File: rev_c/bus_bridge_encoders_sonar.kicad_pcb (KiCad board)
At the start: 2 copper layers, 100 x 50 mm, 52 parts, among them J1 POWER_SELECT, J2 TERMINATE_JUMPER, SW1 MJTP1243, U1 LM2940, U2 LTV-826, U3 LTV-826, U4 LTV-826, U5 754410, U6 LM2940, U7 74HCT08, U8 MCP2562, U9 ATMEGA328_DIP28, X1 16MHz

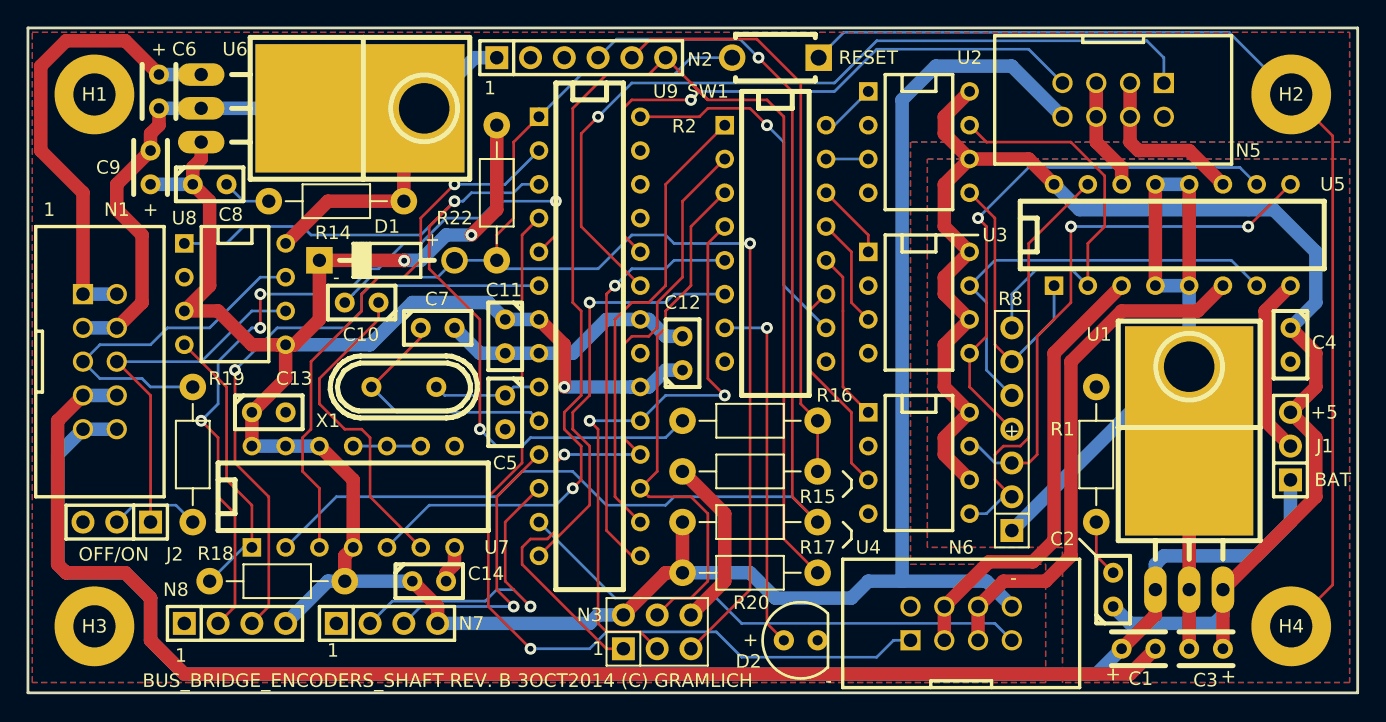
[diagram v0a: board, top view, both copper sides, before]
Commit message: Forgot to commit Rev. C.  Also changed vertical resistors to from pin_header to Resistor_Vertical__100 footprint.
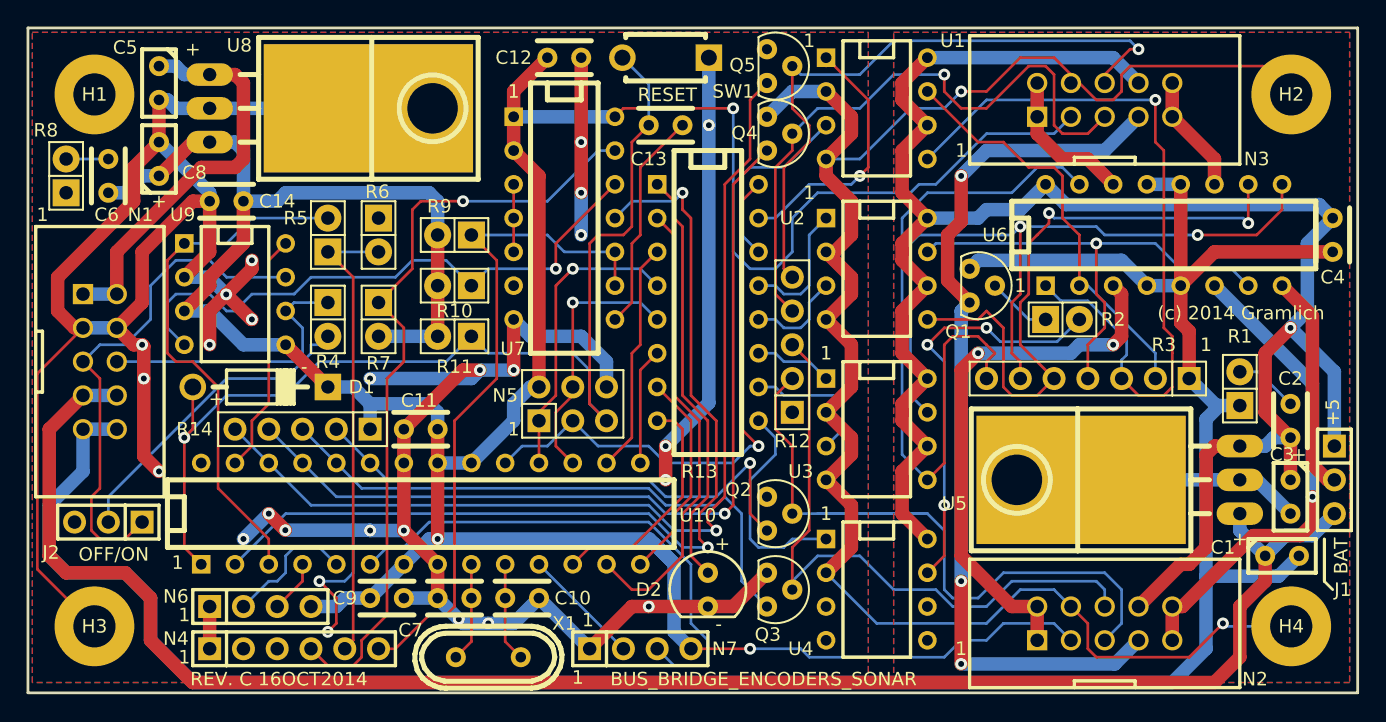
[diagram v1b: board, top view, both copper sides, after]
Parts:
- removed N8: HC_SR04_CONNECTOR, Bus_Bridge_Encoders_Sonar:Pin_Header_Straight_1x04
- removed R15: 22K, Bus_Bridge_Encoders_Sonar:Resistor_Horizontal_400
- removed R16: 33K, Bus_Bridge_Encoders_Sonar:Resistor_Horizontal_400
- removed R17, R18, R20: 100K, Bus_Bridge_Encoders_Sonar:Resistor_Horizontal_400
- removed R19: .47, Bus_Bridge_Encoders_Sonar:Resistor_Horizontal_400
- removed R22: 10K, Bus_Bridge_Encoders_Sonar:Resistor_Horizontal_400
- added N4: FTDI_HEADER, Bus_Bridge_Encoders_Sonar:Pin_Header_Straight_1x06, F.Cu at (120.0, 146.7)
- added Q1: PN2222, Bus_Bridge_Encoders_Sonar:TO92_123, F.Cu at (171.4, 119.4)
- added Q2: PN2222, Bus_Bridge_Encoders_Sonar:TO92_123, F.Cu at (156.2, 136.5)
- added Q3: PN2222, Bus_Bridge_Encoders_Sonar:TO92_123, F.Cu at (156.2, 142.2)
- added Q4: PN2222, Bus_Bridge_Encoders_Sonar:TO92_123, F.Cu at (156.2, 108.0)
- added Q5: PN2222, Bus_Bridge_Encoders_Sonar:TO92_123, F.Cu at (156.2, 102.9)
- added R10: 100K, Bus_Bridge_Encoders_Sonar:Pin_Header_Straight_1x02, F.Cu at (132.1, 119.4)
- added R11: 10K, Bus_Bridge_Encoders_Sonar:Pin_Header_Straight_1x02, F.Cu at (132.1, 123.2)
- added R12: 4K7x4, Bus_Bridge_Encoders_Sonar:Pin_Header_Straight_1x05, F.Cu at (157.5, 123.8)
- added R13: 470_DIP16, Bus_Bridge_Encoders_Sonar:DIP-16__300, F.Cu at (151.1, 120.7)
- added R3: 10Kx6, Bus_Bridge_Encoders_Sonar:Pin_Header_Straight_1x07, F.Cu at (179.7, 126.4)
- added R4: .47, Bus_Bridge_Encoders_Sonar:Pin_Header_Straight_1x02, F.Cu at (122.6, 121.9)
- added R5: 22K, Bus_Bridge_Encoders_Sonar:Pin_Header_Straight_1x02, F.Cu at (122.6, 115.6)
- added R6: 33K, Bus_Bridge_Encoders_Sonar:Pin_Header_Straight_1x02, F.Cu at (126.4, 115.6)
- added R7: 100K, Bus_Bridge_Encoders_Sonar:Pin_Header_Straight_1x02, F.Cu at (126.4, 121.9)
- added R9: 100K, Bus_Bridge_Encoders_Sonar:Pin_Header_Straight_1x02, F.Cu at (132.1, 115.6)
- added U10: ATMEGA328_DIP28, Bus_Bridge_Encoders_Sonar:DIP-28__300, F.Cu at (129.5, 136.5)
- C1, C3: footprint Bus_Bridge_Encoders_Sonar:Capacitor4x3RM2-5_RevB -> Bus_Bridge_Encoders_Sonar:Capacitor3MMDiscRM2.5
- C10: value .1uF -> 18pF; footprint Bus_Bridge_Encoders_Sonar:Capacitor3MMDiscRM2.5 -> Bus_Bridge_Encoders_Sonar:Capacitor4x3RM2-5_RevB
- C11, C12, C13, C14, C2, C4, C7: footprint Bus_Bridge_Encoders_Sonar:Capacitor3MMDiscRM2.5 -> Bus_Bridge_Encoders_Sonar:Capacitor4x3RM2-5_RevB
- C5: value 18pF -> 22uF
- C6, C9: value 22uF -> .1uF
- C8: value .1uF -> 22uF
- N2: value FTDI_HEADER -> MOTOR_ENCODER_CONN_2X5; footprint Bus_Bridge_Encoders_Sonar:Pin_Header_Straight_1x06 -> Bus_Bridge_Encoders_Sonar:Pin_Header_Straight_2x05_Shrouded
- N3: value AVR_ISP_HEADER -> MOTOR_ENCODER_CONN_2X5; footprint Bus_Bridge_Encoders_Sonar:Pin_Header_Straight_2x03 -> Bus_Bridge_Encoders_Sonar:Pin_Header_Straight_2x05_Shrouded
- N5: value MOTOR_ENCODER_CONN -> AVR_ISP_HEADER; footprint Bus_Bridge_Encoders_Sonar:Pin_Header_Straight_2x04_Shrouded -> Bus_Bridge_Encoders_Sonar:Pin_Header_Straight_2x03
- N6: value MOTOR_ENCODER_CONN -> HC_SR04_CONNECTOR; footprint Bus_Bridge_Encoders_Sonar:Pin_Header_Straight_2x04_Shrouded -> Bus_Bridge_Encoders_Sonar:Pin_Header_Straight_1x04
- R1: footprint Bus_Bridge_Encoders_Sonar:Resistor_Horizontal_400 -> Bus_Bridge_Encoders_Sonar:Pin_Header_Straight_1x02
- R14: value .47 -> 3K3x4; footprint Bus_Bridge_Encoders_Sonar:Resistor_Horizontal_400 -> Bus_Bridge_Encoders_Sonar:Pin_Header_Straight_1x05
- R2: value 470 -> 220; footprint Bus_Bridge_Encoders_Sonar:DIP-16__300 -> Bus_Bridge_Encoders_Sonar:Pin_Header_Straight_1x02
- R8: value 10K -> .47; footprint Bus_Bridge_Encoders_Sonar:Pin_Header_Straight_1x07 -> Bus_Bridge_Encoders_Sonar:Pin_Header_Straight_1x02
- U1: value LM2940 -> LTV-826; footprint Bus_Bridge_Encoders_Sonar:TO-220_Neutral123_Horizontal_LargePads -> Bus_Bridge_Encoders_Sonar:DIP-8__300
- U5: value 754410 -> LM2940; footprint Bus_Bridge_Encoders_Sonar:DIP-16__300 -> Bus_Bridge_Encoders_Sonar:TO-220_Neutral123_Horizontal_LargePads
- U6: value LM2940 -> 754410; footprint Bus_Bridge_Encoders_Sonar:TO-220_Neutral123_Horizontal_LargePads -> Bus_Bridge_Encoders_Sonar:DIP-16__300
- U8: value MCP2562 -> LM2940; footprint Bus_Bridge_Encoders_Sonar:DIP-8__300 -> Bus_Bridge_Encoders_Sonar:TO-220_Neutral123_Horizontal_LargePads
- U9: value ATMEGA328_DIP28 -> MCP2562; footprint Bus_Bridge_Encoders_Sonar:DIP-28__300 -> Bus_Bridge_Encoders_Sonar:DIP-8__300
- moved R8 73.6 mm to (102.9, 111.1)
- moved U6 73.0 mm to (185.4, 115.6), turned to 0 degrees
- moved N2 58.0 mm to (181.0, 144.8)
- moved N6 52.7 mm to (117.5, 143.5)
- moved N3 52.3 mm to (181.0, 105.4)
- moved N5 46.6 mm to (141.0, 128.3), turned to 0 degrees
- moved U1 43.2 mm to (163.8, 106.0), turned to 270 degrees
- moved C9 36.9 mm to (127.0, 142.9), turned to 0 degrees
- moved C13 36.8 mm to (148.0, 107.3), turned to 180 degrees
- moved C5 35.9 mm to (109.9, 104.1)
- moved C14 32.4 mm to (114.9, 113.0), turned to 180 degrees
- moved U9 26.9 mm to (115.6, 120.0)
- moved U7 26.3 mm to (140.3, 114.3), turned to 270 degrees
- moved C10 25.3 mm to (137.2, 142.9), turned to 0 degrees
- moved C12 23.9 mm to (140.3, 102.2), turned to 0 degrees
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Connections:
- C1 pad 1: /BPWR -> /Power/BPWR
- C1 pad 2: /BGND -> /Power/BGND
- C10 pad 2: /~RESET -> GND
- C13 pad 1: VCC -> Net-(C13-Pad1)
- C13 pad 2: GND -> /Logic/~RESET
- C2 pad 1: /M5V -> /Power/LED_5V
- C3 pad 1: /M5V -> /Power/LED_5V
- C3 pad 2: /BGND -> /Power/BGND
- C4 pad 1: /M5V -> /Power/LED_5V
- C4 pad 2: /BGND -> /Power/BGND
- C5 pad 1: Net-(C5-Pad1) -> /Logic/LPWR
- C6 pad 1: /LPWR -> VCC
- C6 pad 2: GND -> Net-(C6-Pad2)
- C8 pad 2: Net-(C8-Pad2) -> GND
- D1 pad +: /~RESET -> /Logic/~RESET
- J1 pad 1: /BPWR -> /Power/LED_5V
- J1 pad 2: /MOTOR_POWER -> /Power/MOTOR_POWER
- J1 pad 3: /M5V -> /Power/BPWR
- J2 pad 1: Net-(J2-Pad1) -> /Logic/CANH
- N1 pad 1: /LPWR -> /Logic/LPWR
- N1 pad 10: /BPWR -> /Power/BGND
- N1 pad 2: /LPWR -> /Logic/LPWR
- N1 pad 5: Net-(N1-Pad5) -> /Logic/CANH
- N1 pad 6: Net-(J2-Pad1) -> /Logic/CANL
- N1 pad 7: /BGND -> /Power/BPWR
- N1 pad 8: /BGND -> /Power/BPWR
- N1 pad 9: /BPWR -> /Power/BGND
- N2 pad 1: GND -> /Power/MOTOR1_A
- N2 pad 2: (no net) -> /Power/MOTOR1_A
- N2 pad 3: (no net) -> VCC
- N2 pad 4: Net-(N2-Pad4) -> GND
- N2 pad 5: Net-(N2-Pad5) -> /Logic/ENC1_A
- N2 pad 6: Net-(N2-Pad6) -> /Logic/ENC1_B
- N3 pad 1: /D12 -> /Power/MOTOR2_B
- N3 pad 2: VCC -> /Power/MOTOR2_B
- N3 pad 3: /D13 -> VCC
- N3 pad 4: /D11 -> GND
- N3 pad 5: /~RESET -> /Logic/ENC2_A
- N3 pad 6: GND -> /Logic/ENC2_B
- N5 pad 1: /A0 -> /Logic/D12
- N5 pad 2: GND -> VCC
- N5 pad 3: /M2+ -> /Logic/D13
- N5 pad 4: /M2+ -> /Logic/D11
- N5 pad 5: /M2- -> /Logic/~RESET
- N5 pad 6: /M2- -> GND
- N6 pad 1: /D2 -> GND
- N6 pad 2: GND -> /Logic/D3
- N6 pad 3: /M1+ -> /Logic/D2
- N6 pad 4: /M1+ -> VCC
- N7 pad 2: /D6 -> /Logic/D5
- N7 pad 3: /D5 -> /Logic/D4
- R1 pad 1: /BGND -> /Power/BGND
- R14 pad 1: GND -> VCC
- R14 pad 2: Net-(C8-Pad2) -> /Logic/A0
- R2 pad 1: /D10 -> Net-(Q1-Pad2)
- R2 pad 2: /D12 -> Net-(R2-Pad2)
- R8 pad 1: /BGND -> GND
- R8 pad 2: Net-(R8-Pad2) -> Net-(C6-Pad2)
- SW1 pad 2: /~RESET -> /Logic/~RESET
- U1 pad 1: /BPWR -> /Logic/1A
- U1 pad 2: /BGND -> GND
- U1 pad 3: /M5V -> /Logic/EN12
- U2 pad 1: Net-(R2-Pad16) -> /Logic/2A
- U2 pad 3: Net-(R2-Pad15) -> /Logic/3A
- U2 pad 5: Net-(R8-Pad6) -> Net-(R3-Pad5)
- U2 pad 6: /M5V -> /Power/LED_5V
- U2 pad 7: Net-(R8-Pad7) -> Net-(R3-Pad4)
- U2 pad 8: /M5V -> /Power/LED_5V
- U3 pad 1: Net-(R2-Pad14) -> /Logic/EN34
- U3 pad 3: Net-(R2-Pad13) -> /Logic/4A
- U3 pad 5: Net-(R8-Pad4) -> Net-(R3-Pad7)
- U3 pad 6: /M5V -> /Power/LED_5V
- U3 pad 7: Net-(R8-Pad5) -> Net-(R3-Pad6)
- U3 pad 8: /M5V -> /Power/LED_5V
- U4 pad 1: Net-(R2-Pad12) -> /Logic/ENC_EN
- U4 pad 3: Net-(R2-Pad11) -> (no net)
- U4 pad 4: GND -> (no net)
- U4 pad 5: Net-(R8-Pad2) -> (no net)
- U4 pad 6: /M5V -> (no net)
- U4 pad 7: Net-(R8-Pad3) -> Net-(R2-Pad2)
- U4 pad 8: /M5V -> /Power/LED_5V
- U5 pad 1: Net-(R8-Pad6) -> /Power/BPWR
- U5 pad 2: Net-(R8-Pad7) -> /Power/BGND
- U5 pad 3: /M1+ -> /Power/LED_5V
- U6 pad 1: /LPWR -> Net-(R3-Pad3)
- U6 pad 2: GND -> Net-(R3-Pad2)
- U6 pad 3: VCC -> /Power/MOTOR1_A
- U7 pad 1: Net-(R18-Pad1) -> VCC
- U7 pad 10: Net-(U7-Pad10) -> Net-(N4-Pad6)
- U7 pad 11: Net-(U7-Pad10) -> /Logic/RXD
- U7 pad 12: VCC -> Net-(R10-Pad1)
- U7 pad 13: VCC -> Net-(N4-Pad4)
- U7 pad 2: Net-(N2-Pad4) -> VCC
- U7 pad 3: /RXD -> Net-(U7-Pad3)
- U7 pad 4: VCC -> Net-(U7-Pad3)
- U7 pad 5: Net-(N2-Pad6) -> Net-(U7-Pad3)
- U7 pad 6: Net-(C10-Pad1) -> (no net)
- U7 pad 8: (no net) -> Net-(C13-Pad1)
- U7 pad 9: Net-(U7-Pad10) -> Net-(N4-Pad6)
- U8 pad 1: /TXD -> /Logic/LPWR
- U9 pad 1: /~RESET -> /Logic/TXD
- U9 pad 2: /RXD -> GND
- U9 pad 3: /TXD -> VCC
- U9 pad 4: /D2 -> Net-(R10-Pad1)
- U9 pad 5: /D3 -> VCC
- U9 pad 6: /D4 -> /Logic/CANL
- U9 pad 7: VCC -> /Logic/CANH
- U9 pad 8: GND -> /Logic/A4
- X1 pad 1: Net-(C5-Pad1) -> Net-(C7-Pad1)
- X1 pad 2: Net-(C7-Pad1) -> Net-(C10-Pad1)
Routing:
- net GND: track 185.5 -> 412.4 mm, vias 0 -> 28
- net /Power/BGND: track 0.00 -> 206.4 mm
- net /BGND: track 170.7 -> 0.00 mm
- net /Power/LED_5V: track 0.00 -> 147.9 mm, vias 0 -> 1
- net /Power/BPWR: track 0.00 -> 131.8 mm
- net /BPWR: track 123.5 -> 0.00 mm
- net /M5V: track 112.9 -> 0.00 mm
- net Net-(N2-Pad6): track 102.4 -> 0.00 mm, vias 1 -> 0
- net /~RESET: track 94.8 -> 0.00 mm, vias 1 -> 0
- net Net-(N2-Pad4): track 94.5 -> 0.00 mm, vias 1 -> 0
- net /Logic/~RESET: track 0.00 -> 84.8 mm, vias 0 -> 1
- net /Logic/A3: track 0.00 -> 75.1 mm, vias 0 -> 1
- net /Logic/RXD: track 0.00 -> 72.6 mm, vias 0 -> 2
- net /Power/LED_EN: track 0.00 -> 67.3 mm, vias 0 -> 3
- net /TXD: track 66.9 -> 0.00 mm, vias 2 -> 0
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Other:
- board text added: "(c) 2014 Gramlich"
- board text added: "BUS_BRIDGE_ENCODERS_SONAR"
- board text added: "REV. C 16OCT2014"
- board text removed: "-"
- board text removed: "BUS_BRIDGE_ENCODERS_SHAFT REV. B 3OCT2014 (C) GRAMLICH"
